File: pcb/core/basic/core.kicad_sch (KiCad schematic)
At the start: 31 parts, among them J1 Conn_01x11, J2 Conn_01x11, J3 Conn_01x04, SW1 SW_Push_45deg, SW10 RotaryEncoder_Switch, SW11 RotaryEncoder_Switch, SW12 RotaryEncoder_Switch, SW13 RotaryEncoder_Switch, SW2 SW_Push_45deg, SW3 SW_Push_45deg, SW4 SW_Push_45deg, SW5 SW_Push_45deg, SW6 SW_Push_45deg, SW7 SW_Push_45deg, SW8 SW_Push_45deg, SW9 SW_Push_45deg, U1 Helios

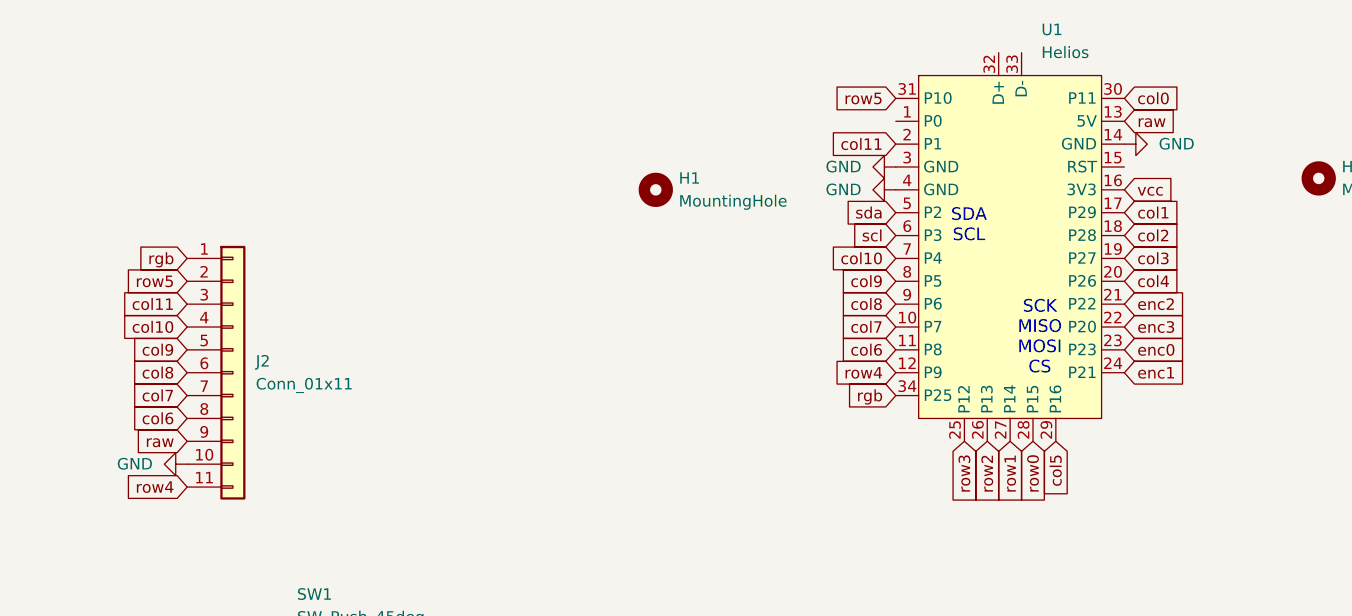
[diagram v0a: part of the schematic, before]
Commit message: switched rgb back to a regular pin and 3v
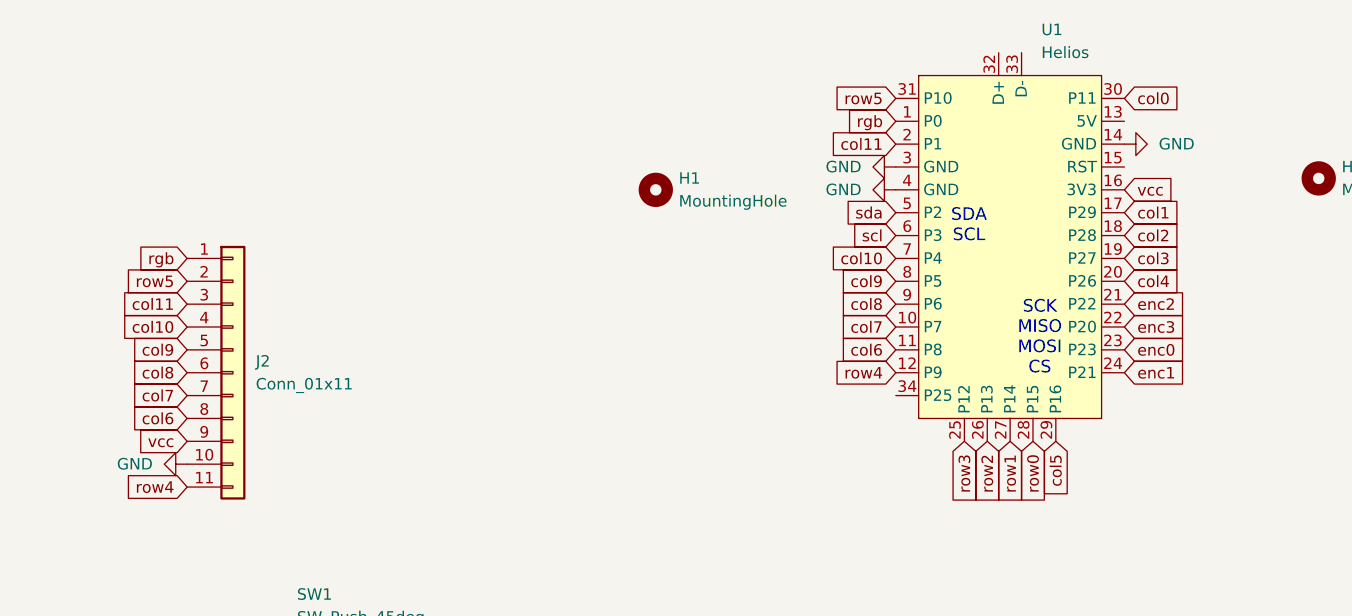
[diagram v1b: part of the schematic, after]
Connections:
- net rgb: now also U1.1 (P0); no longer U1.34 (P25)
- net vcc: now also J2.9 (Pin_9)
- net raw: no longer names the net of U1.13 (5V)
- net raw: no longer J2.9 (Pin_9)
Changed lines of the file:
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@@
 	(global_label "rgb"
 		(shape input)
-		(at 124.46 69.85 180)
-		(fields_autoplaced yes)
-		(effects
-			(font
-				(size 1.27 1.27)
-			)
-			(justify right)
-		)
-		(property "Intersheetrefs" "${INTERSHEET_REFS}"
-			(at 118.3906 69.85 0)
+		(at 124.46 39.37 180)
+		(fields_autoplaced yes)
+		(effects
+			(font
+				(size 1.27 1.27)
+			)
+			(justify right)
+		)
+		(property "Intersheetrefs" "${INTERSHEET_REFS}"
+			(at 118.3906 39.37 0)
 			(effects
 				(font
@@
 		)
 	)
-	(global_label "raw"
+	(global_label "vcc"
 		(shape input)
 		(at 45.72 74.93 180)
@@
 		)
 		(property "Intersheetrefs" "${INTERSHEET_REFS}"
-			(at 39.4691 74.93 0)
+			(at 39.59 74.93 0)
 			(effects
 				(font
@@
 				(hide yes)
 			)
-		)
-	)
-	(global_label "raw"
-		(shape input)
-		(at 149.86 39.37 0)
-		(fields_autoplaced yes)
-		(effects
-			(font
-				(size 1.27 1.27)
-			)
-			(justify left)
-		)
-		(property "Intersheetrefs" "${INTERSHEET_REFS}"
-			(at 156.1109 39.37 0)
-			(effects
-				(font
-					(size 1.27 1.27)
-				)
-				(justify left)
-				(hide yes)
-			)

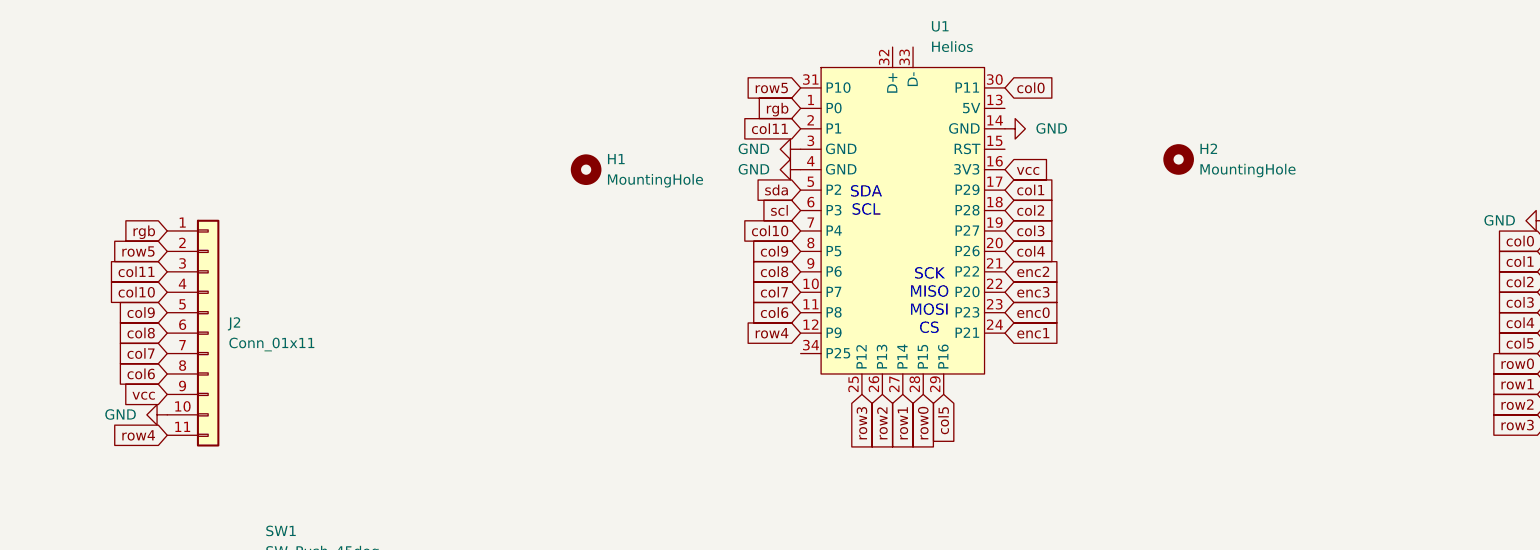
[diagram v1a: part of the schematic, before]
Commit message: added jumpers for 3.3/5v rgb
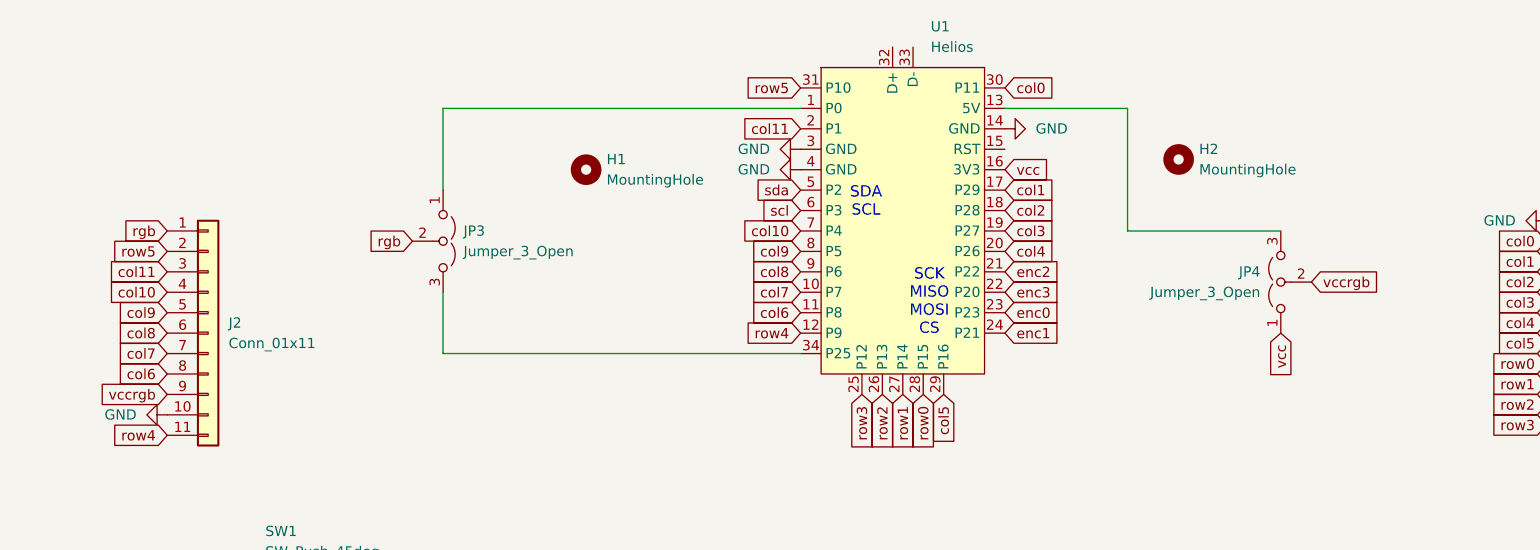
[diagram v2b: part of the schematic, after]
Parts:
- added JP3, JP4: Jumper_3_Open, Jumper:SolderJumper-3_P1.3mm_Open_RoundedPad1.0x1.5mm, symbol Jumper:Jumper_3_Open
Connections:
- net rgb: now also JP3.2 (C); no longer U1.1 (P0)
- net vcc: now also JP4.1 (A); no longer J2.9 (Pin_9)
- net at U1.13 (5V): now also JP4.3 (B)
- net at U1.34 (P25): now also JP3.3 (B)
- new net: JP3.1 (A), U1.1 (P0)
- new net vccrgb: J2.9 (Pin_9), JP4.2 (C)

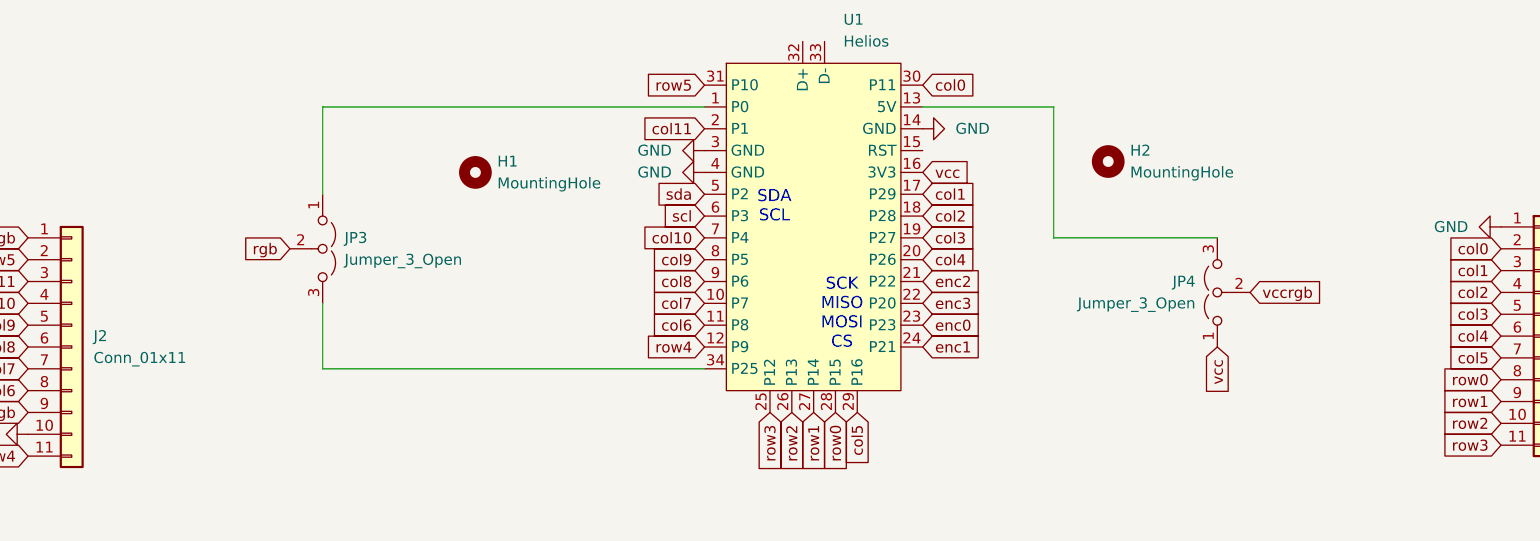
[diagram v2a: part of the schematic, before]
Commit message: moved rgb jumpers to the other side
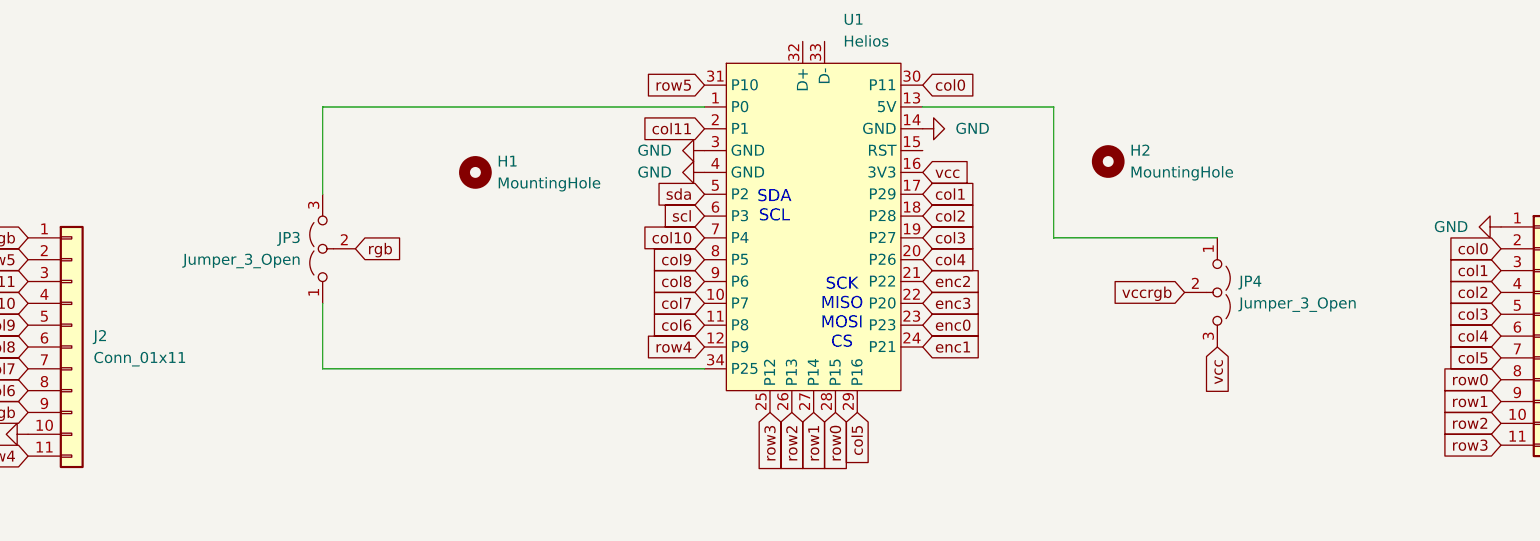
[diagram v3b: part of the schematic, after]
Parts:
- D1, D10, D2, D3, D4, D5, D6, D7, D8, D9: footprint Diode_SMD:D_SOD-123 -> barnacle:D_SOD-123-minimal
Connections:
- net vcc: now also JP4.3 (B); no longer JP4.1 (A)
- net at JP3.1 (A): now also U1.34 (P25); no longer U1.1 (P0)
- net at JP3.3 (B): now also U1.1 (P0); no longer U1.34 (P25)
- net at U1.13 (5V): now also JP4.1 (A); no longer JP4.3 (B)
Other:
- moved on the sheet: JP3, JP4
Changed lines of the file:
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@@
 	(global_label "vccrgb"
 		(shape input)
-		(at 187.96 60.96 0)
+		(at 180.34 60.96 180)
 		(fields_autoplaced yes)
 		(effects
@@
 				(size 1.27 1.27)
 			)
-			(justify left)
+			(justify right)
 		)
 		(property "Intersheetrefs" "${INTERSHEET_REFS}"
-			(at 197.1742 60.96 0)
+			(at 171.1258 60.96 0)
 			(effects
 				(font
 					(size 1.27 1.27)
 				)
-				(justify left)
+				(justify right)
 				(hide yes)
 			)
@@
 	(global_label "rgb"
 		(shape input)
-		(at 76.2 55.88 180)
+		(at 83.82 55.88 0)
 		(fields_autoplaced yes)
 		(effects
@@
 				(size 1.27 1.27)
 			)
-			(justify right)
+			(justify left)
 		)
 		(property "Intersheetrefs" "${INTERSHEET_REFS}"
-			(at 70.1306 55.88 0)
+			(at 89.8894 55.88 0)
 			(effects
 				(font
 					(size 1.27 1.27)
 				)
-				(justify right)
+				(justify left)
 				(hide yes)
 			)
@@
 			)
 		)
-		(property "Footprint" "Diode_SMD:D_SOD-123"
+		(property "Footprint" "barnacle:D_SOD-123-minimal"
 			(at 130.81 175.26 0)
 			(effects
@@
 			)
 		)
-		(property "Footprint" "Diode_SMD:D_SOD-123"
+		(property "Footprint" "barnacle:D_SOD-123-minimal"
 			(at 81.28 138.43 0)
 			(effects
@@
 			)
 		)
-		(property "Footprint" "Diode_SMD:D_SOD-123"
+		(property "Footprint" "barnacle:D_SOD-123-minimal"
 			(at 100.33 138.43 0)
 			(effects
@@
 			)
 		)
-		(property "Footprint" "Diode_SMD:D_SOD-123"
+		(property "Footprint" "barnacle:D_SOD-123-minimal"
 			(at 62.23 138.43 0)
 			(effects
@@
 			)
 		)
-		(property "Footprint" "Diode_SMD:D_SOD-123"
+		(property "Footprint" "barnacle:D_SOD-123-minimal"
 			(at 100.33 175.26 0)
 			(effects
@@
 			)
 		)
-		(property "Footprint" "Diode_SMD:D_SOD-123"
+		(property "Footprint" "barnacle:D_SOD-123-minimal"
 			(at 81.28 113.03 0)
 			(effects
@@
 	(symbol
 		(lib_id "Jumper:Jumper_3_Open")
-		(at 80.01 55.88 270)
+		(at 80.01 55.88 90)
 		(unit 1)
 		(exclude_from_sim yes)
@@
 		(fields_autoplaced yes)
 		(property "Reference" "JP3"
-			(at 82.55 54.6099 90)
+			(at 77.47 54.6099 90)
 			(effects
 				(font
@@
 		)
 		(property "Value" "Jumper_3_Open"
-			(at 82.55 57.1499 90)
+			(at 77.47 57.1499 90)
 			(effects
 				(font
@@
 			)
 		)
-		(property "Footprint" "Diode_SMD:D_SOD-123"
+		(property "Footprint" "barnacle:D_SOD-123-minimal"
 			(at 81.28 175.26 0)
 			(effects
@@
 			)
 		)
-		(property "Footprint" "Diode_SMD:D_SOD-123"
+		(property "Footprint" "barnacle:D_SOD-123-minimal"
 			(at 100.33 113.03 0)
 			(effects
@@
 			)
 		)
-		(property "Footprint" "Diode_SMD:D_SOD-123"
+		(property "Footprint" "barnacle:D_SOD-123-minimal"
 			(at 62.23 175.26 0)
 			(effects
@@
 			)
 		)
-		(property "Footprint" "Diode_SMD:D_SOD-123"
+		(property "Footprint" "barnacle:D_SOD-123-minimal"
 			(at 62.23 113.03 0)
 			(effects
@@
 	(symbol
 		(lib_id "Jumper:Jumper_3_Open")
-		(at 184.15 60.96 90)
+		(at 184.15 60.96 270)
 		(unit 1)
 		(exclude_from_sim yes)
@@
 		(fields_autoplaced yes)
 		(property "Reference" "JP4"
-			(at 181.61 59.6899 90)
+			(at 186.69 59.6899 90)
 			(effects
 				(font
@@
 		)
 		(property "Value" "Jumper_3_Open"
-			(at 181.61 62.2299 90)
+			(at 186.69 62.2299 90)
 			(effects
 				(font
